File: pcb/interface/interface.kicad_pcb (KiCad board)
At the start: 4 copper layers, 49.2 x 49.2 mm, 22 parts, among them J1 Conn_ARM_JTAG_SWD_10, J4 Conn_01x05_Pin, J5 Conn_01x05_Pin, U1 MT6701CT, U2 AP2204K-5.0

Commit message: interface PCB layout
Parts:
- moved C11 23.2 mm to (140.0, 98.4), turned to 180 degrees
- moved C9 1.58 mm to (135.0, 91.0)
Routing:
- net /SWDIO: track 27.6 -> 62.7 mm
- net +5V: track 24.9 -> 57.6 mm, vias 1 -> 2
- net GND: track 28.8 -> 40.4 mm, vias 13 -> 55
- net /SWCLK: track 35.8 -> 44.4 mm
- net /VTarget: track 24.7 -> 28.5 mm
- net VBUS: track 6.16 -> 8.08 mm, vias 11 -> 12
- net (no net): track 0.00 -> 0.40 mm, vias 0 -> 4
- added copper zone on F.Cu, net GND

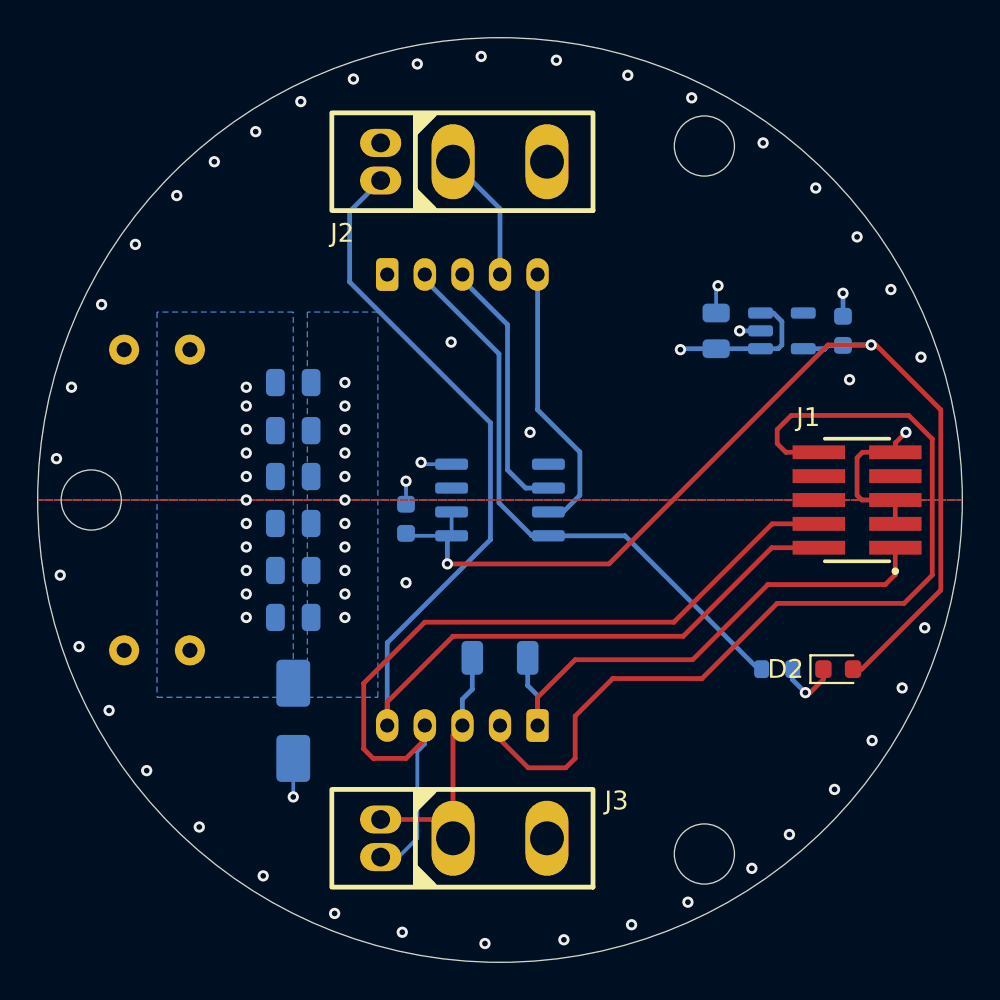
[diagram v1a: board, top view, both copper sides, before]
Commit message: fix reversed connector
and add a TVS diode
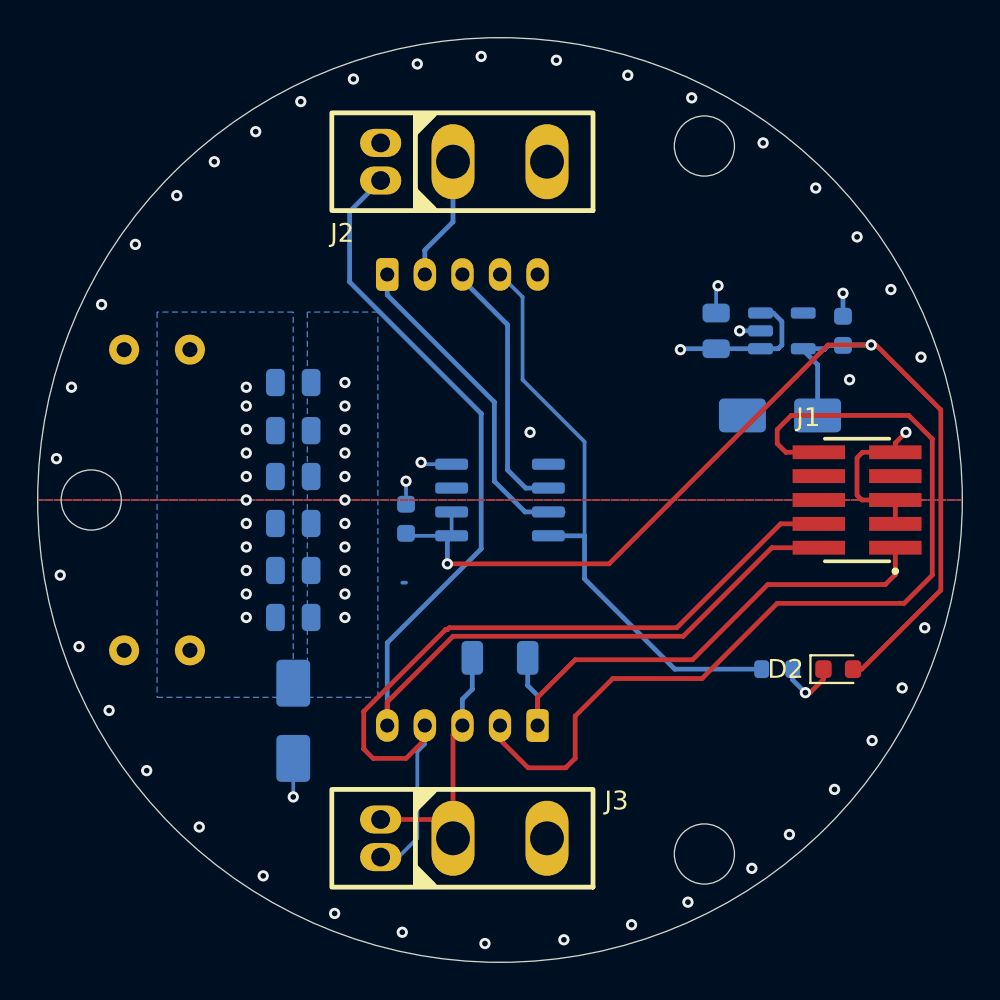
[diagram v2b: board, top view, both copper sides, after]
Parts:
- added D3: SMAJ6.0A, Diode_SMD:D_SMA, B.Cu at (154.9, 85.5)
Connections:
- J5 pad 1: VBUS -> /SSI_CK
- J5 pad 2: /SSI_CSN -> GND
- J5 pad 4: GND -> /SSI_CSN
- J5 pad 5: /SSI_CK -> VBUS
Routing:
- net +5V: track 57.6 -> 61.5 mm
- net /SSI_CK: track 14.7 -> 17.7 mm
- net /SWCLK: track 44.4 -> 43.5 mm
- net (no net): vias 4 -> 2

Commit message: clearer pcb labeling
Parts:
- moved C11 7.60 mm to (147.1, 101.1), turned to 0 degrees
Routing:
- net GND: track 40.2 -> 36.4 mm
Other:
- board text added: "+"
- board text added: "-"
- board text added: "DIR"
- board text added: "GND"
- board text added: "Motor Leads"
- board text added: "P"
- board text added: "PROG"
- board text added: "PWM"
- board text added: "R"
- board text added: "RX"
- board text added: "S"
- board text added: "SWD"
- board text added: "TACH"
- board text added: "TX"
- board text added: "V+"

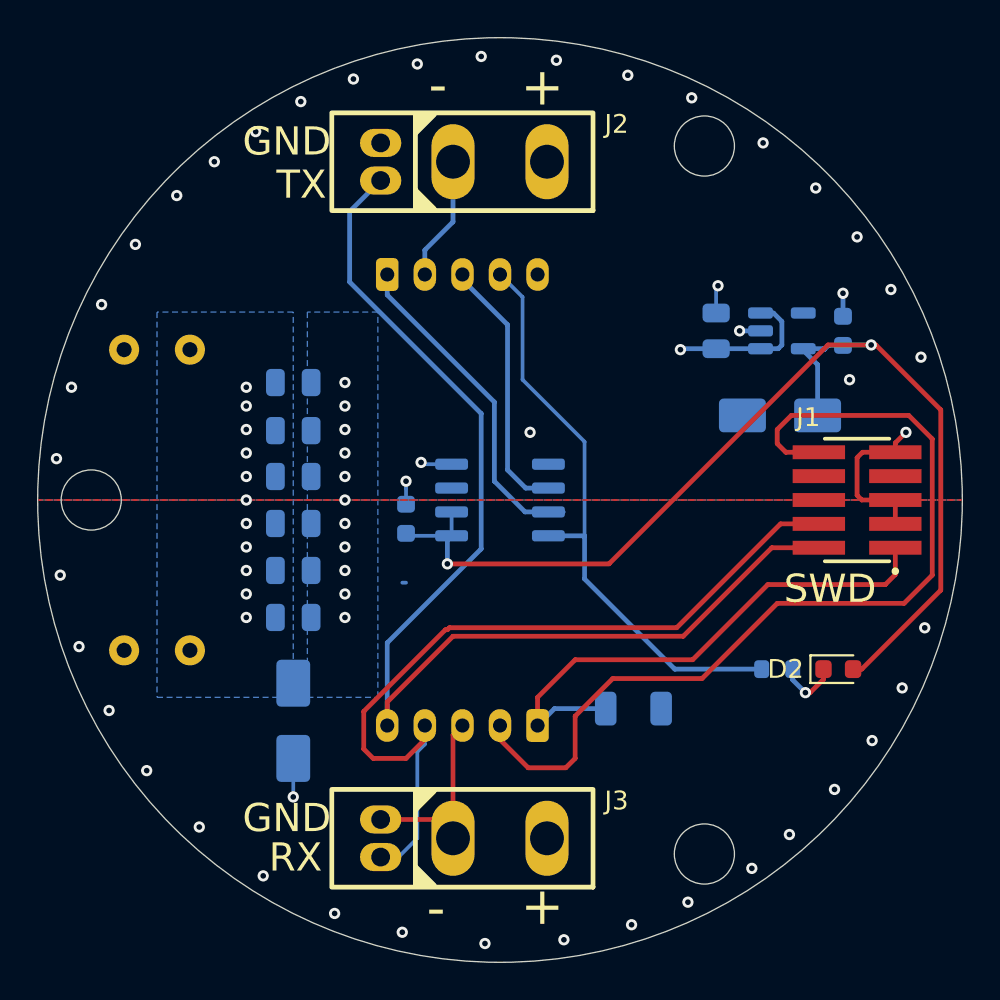
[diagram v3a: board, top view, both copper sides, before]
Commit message: as-ordered V2 interface boards
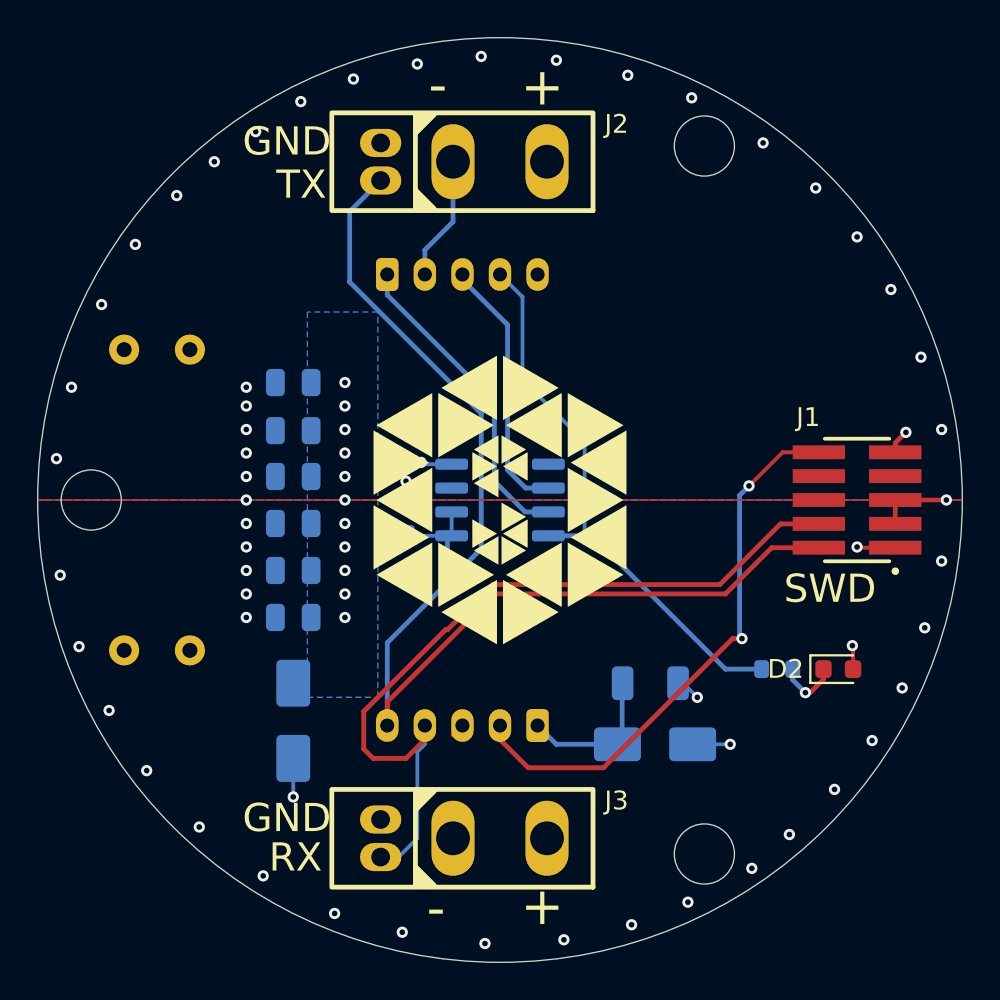
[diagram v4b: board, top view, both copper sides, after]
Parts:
- removed C10: 10uF, Capacitor_SMD:C_0805_2012Metric
- removed C12: 10uF, Capacitor_SMD:C_0603_1608Metric
- removed U2: AP2204K-5.0, Package_TO_SOT_SMD:SOT-23-5
- moved D3 18.7 mm to (148.2, 103.0), turned to 0 degrees
- moved C11 1.62 mm to (148.0, 99.8)
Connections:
- C11 pad 1: /VTarget -> +5V
- J1 pad 1: /VTarget -> +5V
- J4 pad 1: /VTarget -> +5V
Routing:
- net +5V: track 61.5 -> 16.6 mm, vias 2 -> 3
- net /VTarget: track 28.7 -> 0.00 mm
- net /Reset: track 49.4 -> 29.9 mm, vias 0 -> 2
- net GND: track 36.4 -> 20.6 mm, vias 55 -> 57
- net VBUS: track 8.08 -> 0.00 mm, vias 12 -> 11
- net /SSI_CSN: track 31.4 -> 30.1 mm
- net /SWCLK: track 43.5 -> 42.6 mm
- net /SSI_CK: track 17.7 -> 16.9 mm
- net (no net): track 0.40 -> 0.00 mm, vias 2 -> 0
- added copper zone on In2.Cu, net +5V
